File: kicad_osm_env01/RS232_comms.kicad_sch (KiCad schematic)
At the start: 17 parts, among them U19 MAX3223IPWR

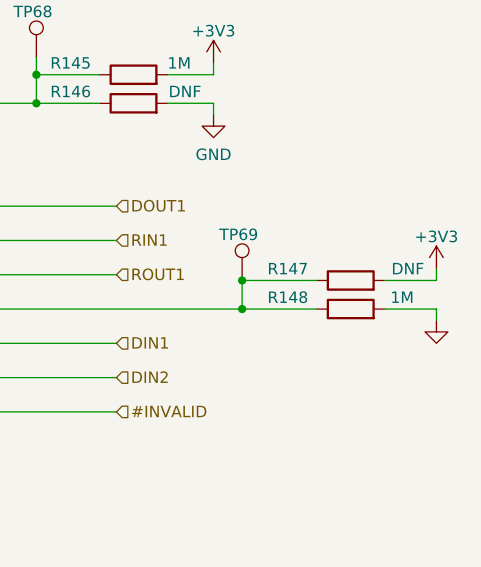
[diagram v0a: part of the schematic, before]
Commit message: updated changes document with xnor power mod and updated schematics with mods so far for osm rev c
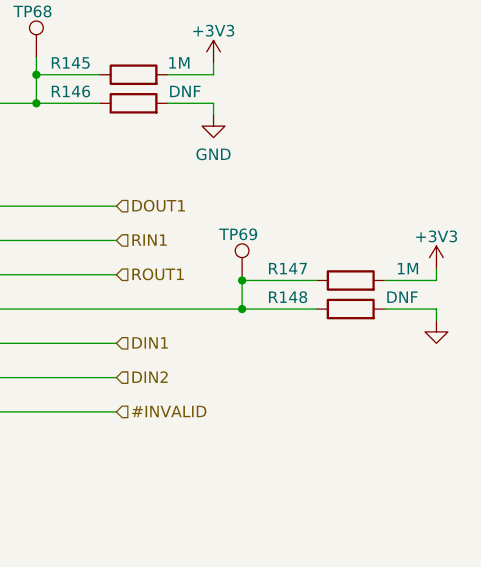
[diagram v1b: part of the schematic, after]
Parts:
- R147: value DNF -> 1M
- R148: value 1M -> DNF
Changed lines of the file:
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@@
     (in_bom yes) (on_board yes)
     (property "Reference" "R147" (id 0) (at 200.66 102.235 90))
-    (property "Value" "DNF" (id 1) (at 213.995 102.235 90))
+    (property "Value" "1M" (id 1) (at 213.995 102.235 90))
     (property "Footprint" "Resistor_SMD:R_0603_1608Metric" (id 2) (at 207.645 105.283 90)
       (effects (font (size 1.27 1.27)) hide)
@@
     (in_bom yes) (on_board yes)
     (property "Reference" "R148" (id 0) (at 200.66 105.41 90))
-    (property "Value" "1M" (id 1) (at 213.36 105.41 90))
+    (property "Value" "DNF" (id 1) (at 213.36 105.41 90))
     (property "Footprint" "Resistor_SMD:R_0603_1608Metric" (id 2) (at 207.645 108.458 90)
       (effects (font (size 1.27 1.27)) hide)

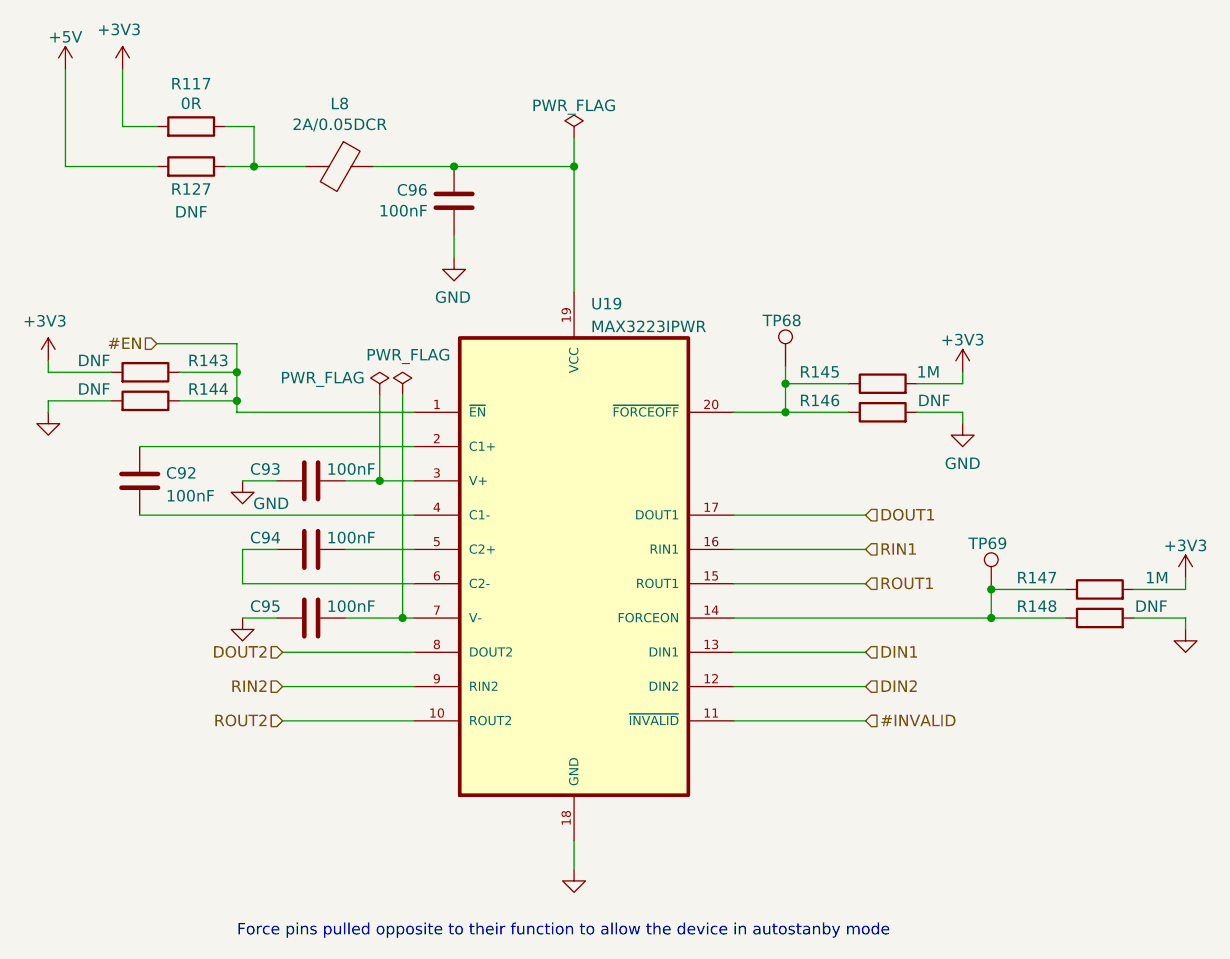
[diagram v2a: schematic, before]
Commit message: removed io module and 5V regulator
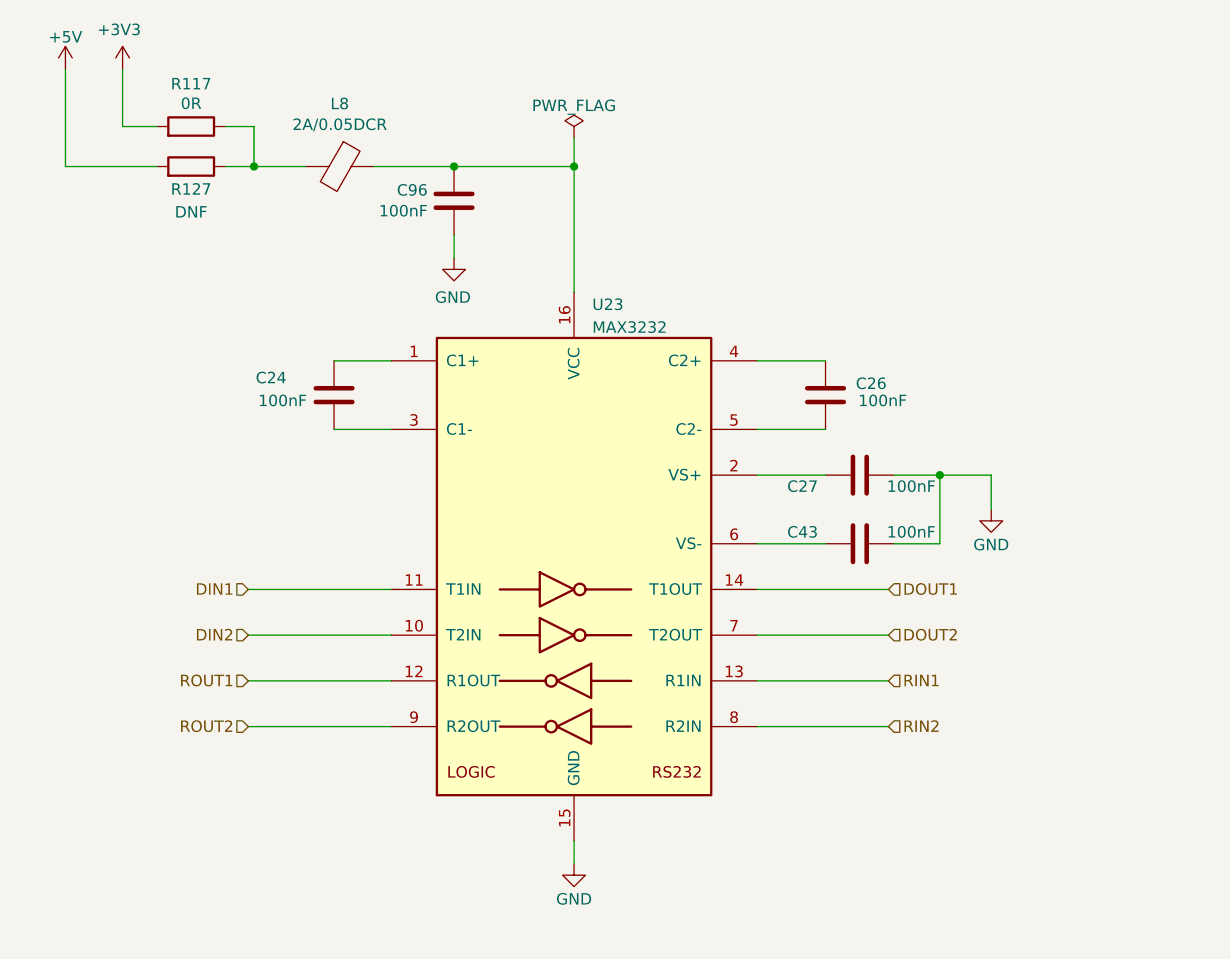
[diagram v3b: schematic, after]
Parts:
- removed C92, C93, C94, C95: 100nF, Capacitor_SMD:C_0402_1005Metric, symbol Device:C
- removed R143, R144, R146, R148: DNF, Resistor_SMD:R_0603_1608Metric, symbol Device:R
- removed R145, R147: 1M, Resistor_SMD:R_0603_1608Metric, symbol Device:R
- removed TP68, TP69: Test_Point, TestPoint:TestPoint_THTPad_D1.0mm_Drill0.5mm, symbol Connector:TestPoint
- removed U19: MAX3223IPWR, Package_SO:TSSOP-20_4.4x6.5mm_P0.65mm, symbol Devtank:MAX3223IPWR
- added C24, C26, C27, C43: 100nF, Capacitor_SMD:C_0402_1005Metric, symbol Device:C
- added U23: MAX3232, Package_SO:TSSOP-16_4.4x5mm_P0.65mm, symbol Interface_UART:MAX3232
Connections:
- net DIN1: now also U23.11 (T1IN)
- net DIN2: now also U23.10 (T2IN)
- net DOUT1: now also U23.14 (T1OUT)
- net DOUT2: now also U23.7 (T2OUT)
- net GND: now also C27.1, C43.1, U23.15 (GND)
- net RIN1: now also U23.13 (R1IN)
- net RIN2: now also U23.8 (R2IN)
- net ROUT1: now also U23.12 (R1OUT)
- net ROUT2: now also U23.9 (R2OUT)
- net at C96.1, L8.1: now also U23.16 (VCC)
- new net: C26.1, U23.5 (C2-)
- new net: C26.2, U23.4 (C2+)
- new net: C43.2, U23.6 (VS-)
- new net: C27.2, U23.2 (VS+)
- new net: C24.1, U23.3 (C1-)
- new net: C24.2, U23.1 (C1+)
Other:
- note removed: "Force pins pulled opposite to their function to allow the device in autostanby mode"

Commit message: assigned all footprints
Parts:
- C24, C26, C27, C43: Characteristics X5R -> (none); Voltage 10V -> 50V
- C96: Voltage (none) -> 50V
- R117, R127: footprint Resistor_SMD:R_0603_1608Metric -> Resistor_SMD:R_0402_1005Metric
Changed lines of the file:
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@@
   (title_block
     (title "Open Smart Monitor")
-    (date "2022-09-26")
-    (rev "C")
+    (date "2023-09-29")
+    (rev "C.2")
     (company "Devtank LTD")
     (comment 1 "Part No: 304-010")
@@
       (effects (font (size 1.27 1.27)))
     )
-    (property "Footprint" "Resistor_SMD:R_0603_1608Metric" (at 106.68 53.848 90)
+    (property "Footprint" "Resistor_SMD:R_0402_1005Metric" (at 106.68 53.848 90)
       (effects (font (size 1.27 1.27)) hide)
     )
@@
     )
     (property "Datasheet" "" (at 135.89 60.325 0)
+      (effects (font (size 1.27 1.27)) hide)
+    )
+    (property "Voltage" "50V" (at 135.89 60.325 0)
       (effects (font (size 1.27 1.27)) hide)
     )
@@
       (effects (font (size 1.27 1.27)) hide)
     )
-    (property "Datasheet" "~" (at 177.165 81.915 0)
-      (effects (font (size 1.27 1.27)) hide)
-    )
-    (property "Voltage" "10V" (at 177.165 81.915 0)
-      (effects (font (size 1.27 1.27)) hide)
-    )
-    (property "Characteristics" "X5R" (at 177.165 81.915 0)
+    (property "Datasheet" "" (at 177.165 81.915 0)
+      (effects (font (size 1.27 1.27)) hide)
+    )
+    (property "Voltage" "50V" (at 177.165 81.915 0)
+      (effects (font (size 1.27 1.27)) hide)
+    )
+    (property "Characteristics" "" (at 177.165 81.915 0)
       (effects (font (size 1.27 1.27)) hide)
     )
@@
       (effects (font (size 1.27 1.27)))
     )
-    (property "Footprint" "Resistor_SMD:R_0603_1608Metric" (at 106.68 58.293 90)
+    (property "Footprint" "Resistor_SMD:R_0402_1005Metric" (at 106.68 58.293 90)
       (effects (font (size 1.27 1.27)) hide)
     )
@@
       (effects (font (size 1.27 1.27)) hide)
     )
-    (property "Datasheet" "~" (at 180.975 98.425 0)
-      (effects (font (size 1.27 1.27)) hide)
-    )
-    (property "Voltage" "10V" (at 180.975 98.425 0)
-      (effects (font (size 1.27 1.27)) hide)
-    )
-    (property "Characteristics" "X5R" (at 180.975 98.425 0)
+    (property "Datasheet" "" (at 180.975 98.425 0)
+      (effects (font (size 1.27 1.27)) hide)
+    )
+    (property "Voltage" "50V" (at 180.975 98.425 0)
+      (effects (font (size 1.27 1.27)) hide)
+    )
+    (property "Characteristics" "" (at 180.975 98.425 0)
       (effects (font (size 1.27 1.27)) hide)
     )
@@
       (effects (font (size 1.27 1.27)) hide)
     )
-    (property "Datasheet" "~" (at 180.975 90.805 0)
-      (effects (font (size 1.27 1.27)) hide)
-    )
-    (property "Voltage" "10V" (at 180.975 90.805 0)
-      (effects (font (size 1.27 1.27)) hide)
-    )
-    (property "Characteristics" "X5R" (at 180.975 90.805 0)
+    (property "Datasheet" "" (at 180.975 90.805 0)
+      (effects (font (size 1.27 1.27)) hide)
+    )
+    (property "Voltage" "50V" (at 180.975 90.805 0)
+      (effects (font (size 1.27 1.27)) hide)
+    )
+    (property "Characteristics" "" (at 180.975 90.805 0)
       (effects (font (size 1.27 1.27)) hide)
     )
@@
       (effects (font (size 1.27 1.27)) hide)
     )
-    (property "Datasheet" "~" (at 122.555 81.915 0)
-      (effects (font (size 1.27 1.27)) hide)
-    )
-    (property "Voltage" "10V" (at 122.555 81.915 0)
-      (effects (font (size 1.27 1.27)) hide)
-    )
-    (property "Characteristics" "X5R" (at 122.555 81.915 0)
-      (effects (font (size 1.27 1.27)) hide)
-    )
+    (property "Datasheet" "" (at 122.555 81.915 0)
+      (effects (font (size 1.27 1.27)) hide)
+    )
+    (property "Voltage" "50V" (at 122.555 81.915 0)
+      (effects (font (size 1.27 1.27)) hide)
+    )
+    (property "Characteristics" "" (at 122.555 81.915 0)
+      (effects (font (size 1.27 1.27)) hide)
+    )

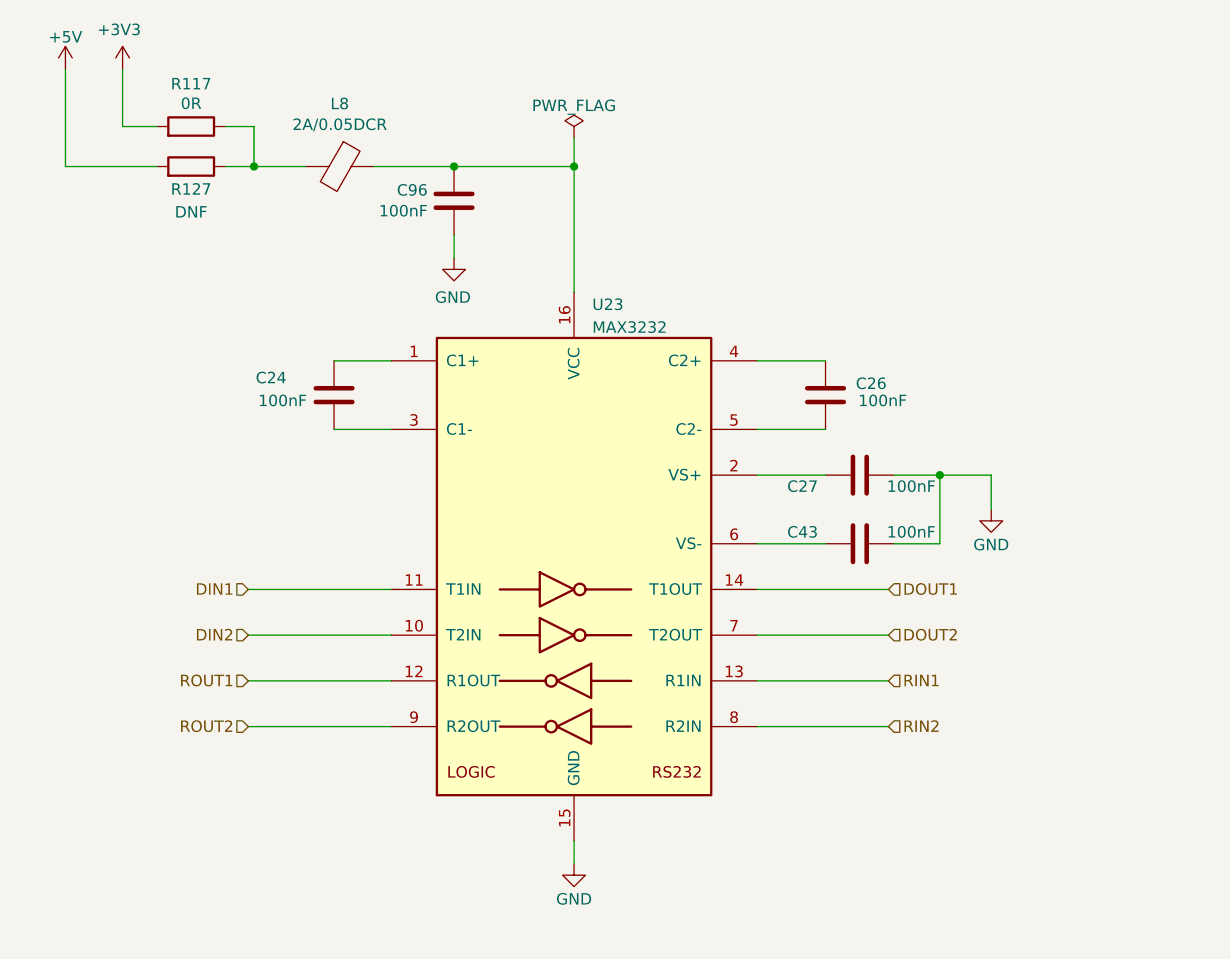
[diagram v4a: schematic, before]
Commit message: layout updated with a few ic packages due to errors, silk screen tidy up, logos added, minor update to rs232 schematics and pinmap to stm
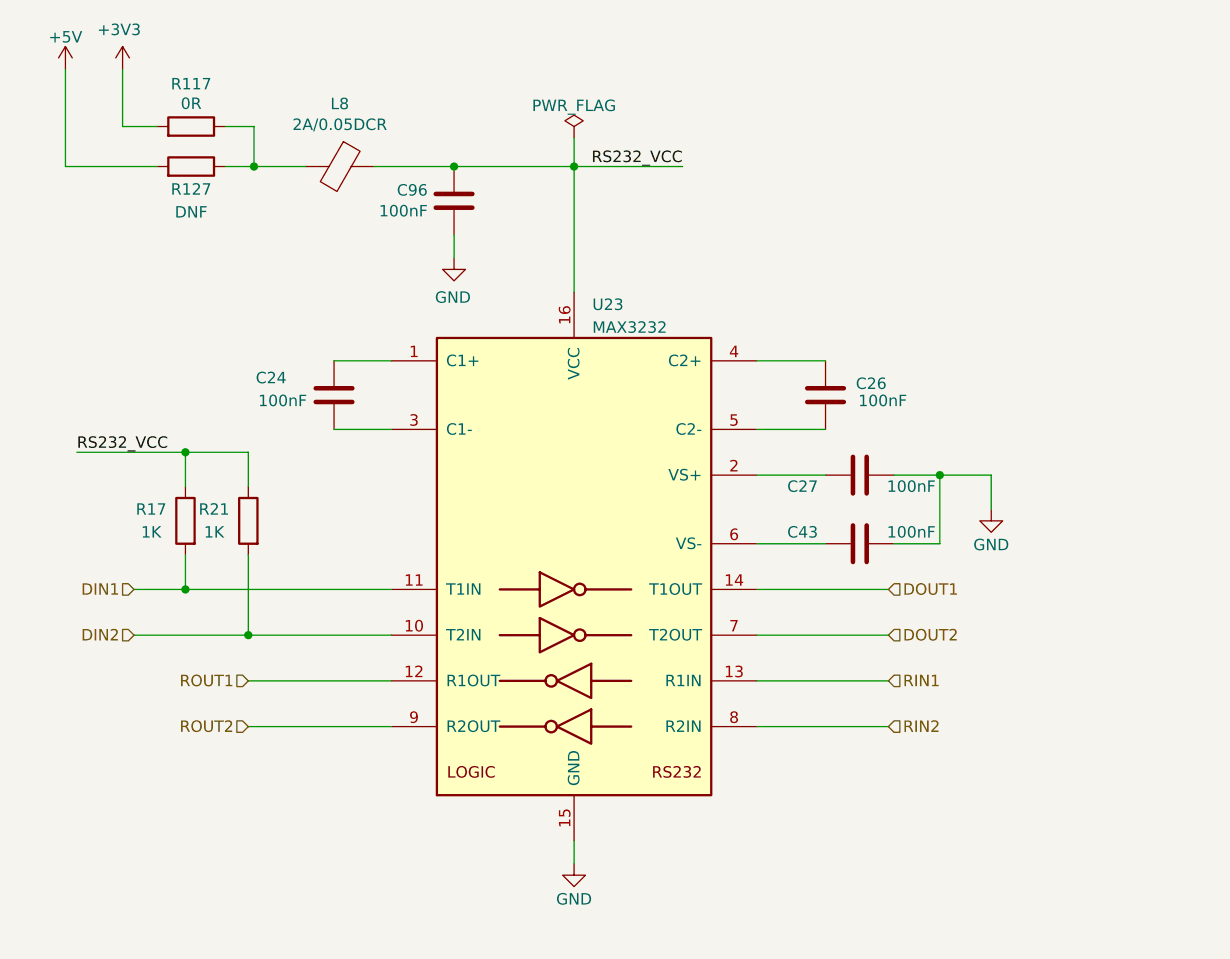
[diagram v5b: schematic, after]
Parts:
- added R17, R21: 1K, Resistor_SMD:R_0402_1005Metric, symbol Device:R
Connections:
- net DIN1: now also R17.2
- net DIN2: now also R21.2
- net RS232_VCC: now reaches C96.1, L8.1, U23.16 (VCC)
- net RS232_VCC: now also R17.1, R21.1
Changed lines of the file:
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@@
   (junction (at 135.89 56.515) (diameter 0) (color 0 0 0 0)
   )
+  (junction (at 106.045 88.265) (diameter 0) (color 0 0 0 0)
+  )
+  (junction (at 106.045 103.505) (diameter 0) (color 0 0 0 0)
+  )
+  (junction (at 113.03 108.585) (diameter 0) (color 0 0 0 0)
+  )
   (wire (pts (xy 113.665 52.07) (xy 113.665 56.515))
     (stroke (width 0) (type default))
@@
     (stroke (width 0) (type default))
   )
+  (wire (pts (xy 106.045 92.075) (xy 106.045 88.265))
+    (stroke (width 0) (type default))
+  )
   (wire (pts (xy 113.03 113.665) (xy 128.905 113.665))
     (stroke (width 0) (type default))
@@
     (stroke (width 0) (type default))
   )
-  (wire (pts (xy 113.03 103.505) (xy 128.905 103.505))
+  (wire (pts (xy 100.33 103.505) (xy 106.045 103.505))
     (stroke (width 0) (type default))
   )
@@
     (stroke (width 0) (type default))
   )
+  (wire (pts (xy 113.03 88.265) (xy 113.03 92.075))
+    (stroke (width 0) (type default))
+  )
   (wire (pts (xy 127 56.515) (xy 135.89 56.515))
     (stroke (width 0) (type default))
@@
     (stroke (width 0) (type default))
   )
-  (wire (pts (xy 128.905 108.585) (xy 113.03 108.585))
+  (wire (pts (xy 100.33 108.585) (xy 113.03 108.585))
     (stroke (width 0) (type default))
   )
@@
     (stroke (width 0) (type default))
   )
+  (wire (pts (xy 106.045 88.265) (xy 93.98 88.265))
+    (stroke (width 0) (type default))
+  )
+  (wire (pts (xy 106.045 103.505) (xy 128.905 103.505))
+    (stroke (width 0) (type default))
+  )
   (wire (pts (xy 92.71 45.72) (xy 92.71 56.515))
     (stroke (width 0) (type default))
   )
+  (wire (pts (xy 113.03 99.695) (xy 113.03 108.585))
+    (stroke (width 0) (type default))
+  )
+  (wire (pts (xy 106.045 88.265) (xy 113.03 88.265))
+    (stroke (width 0) (type default))
+  )
   (wire (pts (xy 184.15 113.665) (xy 169.545 113.665))
     (stroke (width 0) (type default))
@@
     (stroke (width 0) (type default))
   )
+  (wire (pts (xy 149.225 56.515) (xy 161.29 56.515))
+    (stroke (width 0) (type default))
+  )
   (wire (pts (xy 184.15 103.505) (xy 169.545 103.505))
     (stroke (width 0) (type default))
   )
+  (wire (pts (xy 113.03 108.585) (xy 128.905 108.585))
+    (stroke (width 0) (type default))
+  )
   (wire (pts (xy 99.06 45.72) (xy 99.06 52.07))
     (stroke (width 0) (type default))
@@
     (stroke (width 0) (type default))
   )
+  (wire (pts (xy 106.045 99.695) (xy 106.045 103.505))
+    (stroke (width 0) (type default))
+  )
   (wire (pts (xy 149.225 53.34) (xy 149.225 56.515))
     (stroke (width 0) (type default))
@@
   (wire (pts (xy 119.38 56.515) (xy 113.665 56.515))
     (stroke (width 0) (type default))
+  )
+  (label "RS232_VCC" (at 93.98 88.265 0) (fields_autoplaced)
+    (effects (font (size 1.27 1.27)) (justify left bottom))
+  )
+  (label "RS232_VCC" (at 161.29 56.515 180) (fields_autoplaced)
+    (effects (font (size 1.27 1.27)) (justify right bottom))
   )
   (hierarchical_label "ROUT2" (shape input) (at 113.03 118.745 180) (fields_autoplaced)
@@
     (effects (font (size 1.27 1.27)) (justify right))
   )
-  (hierarchical_label "DIN2" (shape input) (at 113.03 108.585 180) (fields_autoplaced)
+  (hierarchical_label "DIN2" (shape input) (at 100.33 108.585 180) (fields_autoplaced)
     (effects (font (size 1.27 1.27)) (justify right))
   )
-  (hierarchical_label "DIN1" (shape input) (at 113.03 103.505 180) (fields_autoplaced)
+  (hierarchical_label "DIN1" (shape input) (at 100.33 103.505 180) (fields_autoplaced)
     (effects (font (size 1.27 1.27)) (justify right))
   )
@@
         )
       )
+    )
+  )
+  (symbol (lib_id "Device:R") (at 113.03 95.885 0) (mirror y) (unit 1)
+    (in_bom yes) (on_board yes) (dnp no)
+    (property "Reference" "R21" (at 109.22 94.615 0)
+      (effects (font (size 1.27 1.27)))
+    )
+    (property "Value" "1K" (at 109.22 97.155 0)
+      (effects (font (size 1.27 1.27)))
+    )
+    (property "Footprint" "Resistor_SMD:R_0402_1005Metric" (at 114.808 95.885 90)
+      (effects (font (size 1.27 1.27)) hide)
+    )
+    (property "Datasheet" "" (at 113.03 95.885 0)
+      (effects (font (size 1.27 1.27)) hide)
+    )
+    (pin "1")
+    (pin "2")
+    (instances
+      (project "OSM_env01"
+        (path "/ab8b0540-9c9f-4195-88f5-7bed0b0a8ed6/b9a077bb-8b65-41fb-9650-f17f6dddad7c"
+          (reference "R21") (unit 1)
+        )
+      )
+    )
+  )
+  (symbol (lib_id "Device:R") (at 106.045 95.885 0) (mirror y) (unit 1)
+    (in_bom yes) (on_board yes) (dnp no)
+    (property "Reference" "R17" (at 102.235 94.615 0)
+      (effects (font (size 1.27 1.27)))
+    )
+    (property "Value" "1K" (at 102.235 97.155 0)
+      (effects (font (size 1.27 1.27)))
+    )
+    (property "Footprint" "Resistor_SMD:R_0402_1005Metric" (at 107.823 95.885 90)
+      (effects (font (size 1.27 1.27)) hide)
+    )
+    (property "Datasheet" "" (at 106.045 95.885 0)
+      (effects (font (size 1.27 1.27)) hide)
+    )
+    (pin "1")
+    (pin "2")
+    (instances
+      (project "OSM_env01"
+        (path "/ab8b0540-9c9f-4195-88f5-7bed0b0a8ed6/b9a077bb-8b65-41fb-9650-f17f6dddad7c"
+          (reference "R17") (unit 1)
+        )
+      )
